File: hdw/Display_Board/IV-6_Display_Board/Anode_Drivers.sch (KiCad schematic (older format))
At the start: 48 parts

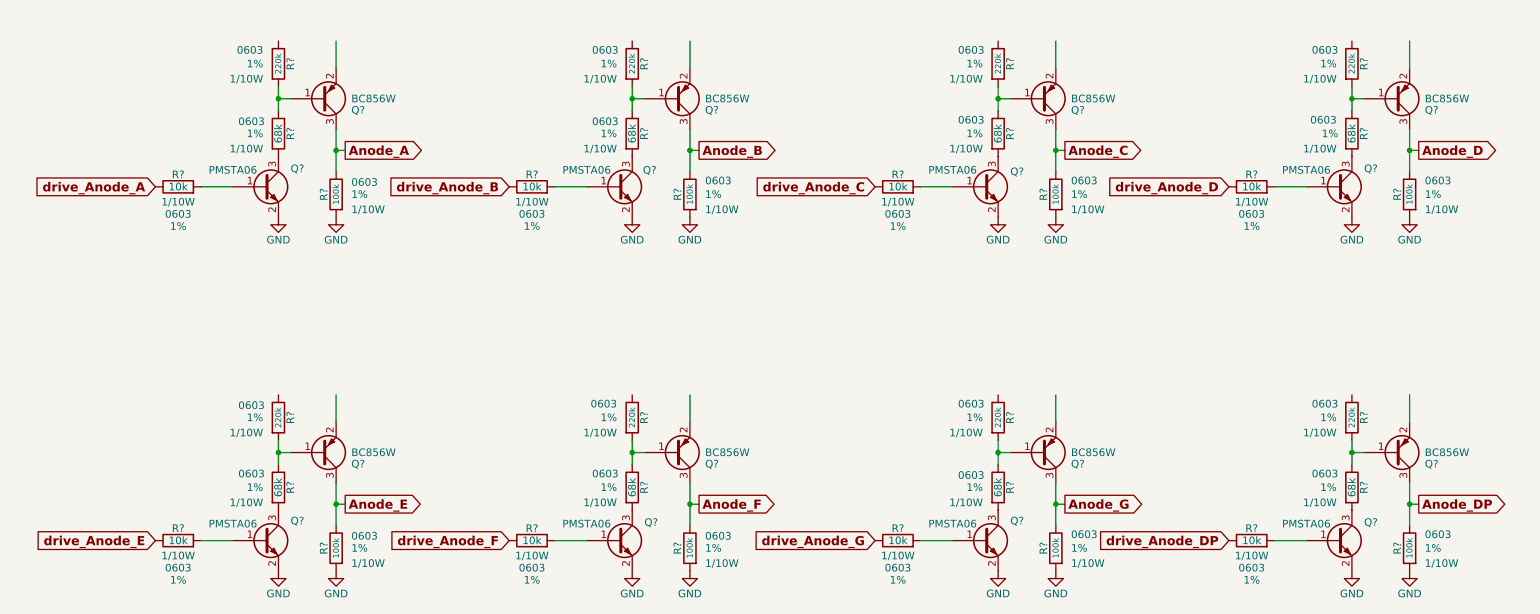
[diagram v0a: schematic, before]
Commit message: Started IV-6 display board, continued logic board development
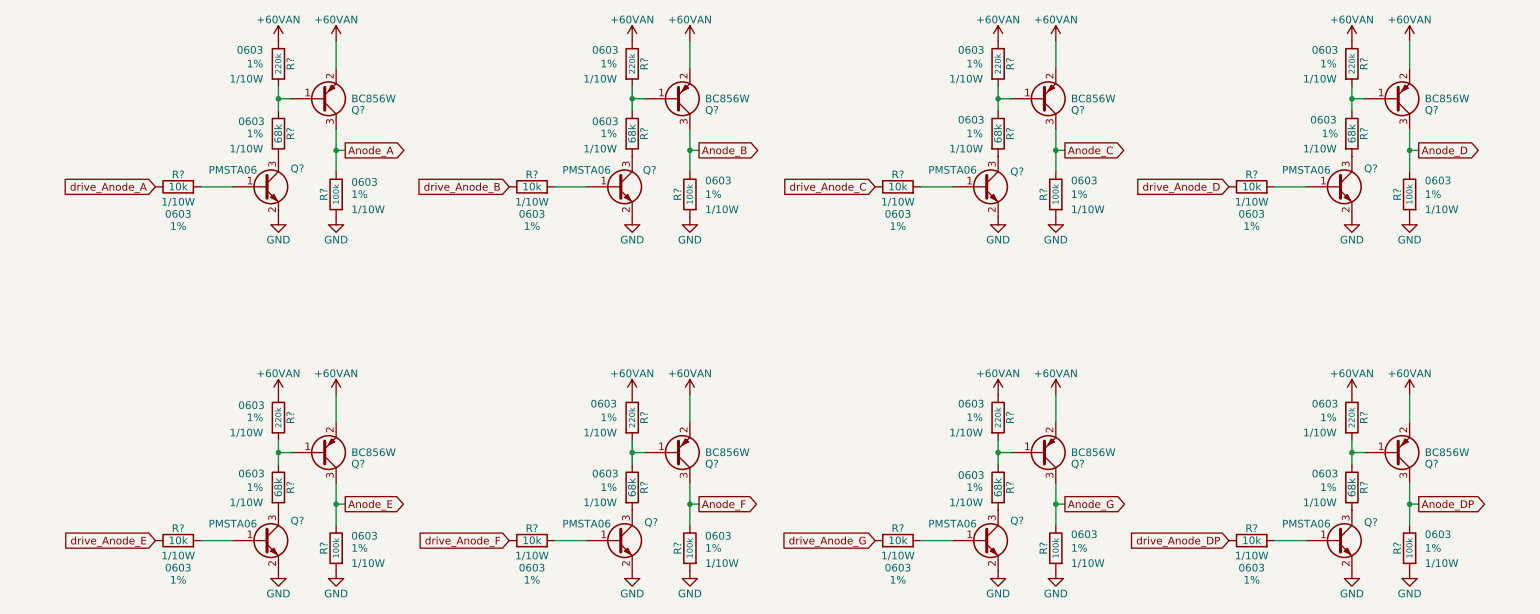
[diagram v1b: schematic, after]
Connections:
- net labels added: +60VAN
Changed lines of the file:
@@
 EESchema Schematic File Version 4
-EELAYER 29 0
+EELAYER 30 0
 EELAYER END
 $Descr A 11000 8500
 encoding utf-8
-Sheet 2 3
+Sheet 2 5
 Title "VFD Clock"
 Date "2019-04-11"
@@
 Wire Wire Line
 	1800 2500 1590 2500
-Text GLabel 1290 2500 0    60   Input ~ 12
+Text GLabel 1290 2500 0    50   Input ~ 0
 drive_Anode_A
-Text GLabel 3620 2500 0    60   Input ~ 12
+Text GLabel 3620 2500 0    50   Input ~ 0
 drive_Anode_B
-Text GLabel 6030 2500 0    60   Input ~ 12
+Text GLabel 6030 2500 0    50   Input ~ 0
 drive_Anode_C
-Text GLabel 8360 2500 0    60   Input ~ 12
+Text GLabel 8360 2500 0    50   Input ~ 0
 drive_Anode_D
-Text GLabel 1290 4830 0    60   Input ~ 12
+Text GLabel 1290 4830 0    50   Input ~ 0
 drive_Anode_E
-Text GLabel 3620 4830 0    60   Input ~ 12
+Text GLabel 3620 4830 0    50   Input ~ 0
 drive_Anode_F
-Text GLabel 6030 4830 0    60   Input ~ 12
+Text GLabel 6030 4830 0    50   Input ~ 0
 drive_Anode_G
-Text GLabel 8360 4830 0    60   Input ~ 12
+Text GLabel 8360 4830 0    50   Input ~ 0
 drive_Anode_DP
-Text GLabel 2540 2260 2    60   Output ~ 12
-Anode_A
 Wire Wire Line
 	2540 2260 2480 2260
@@
 Wire Wire Line
 	4130 2500 3920 2500
-Text GLabel 4870 2260 2    60   Output ~ 12
+Text GLabel 4870 2260 2    50   Output ~ 0
 Anode_B
 Wire Wire Line
@@
 Wire Wire Line
 	6540 2500 6330 2500
-Text GLabel 7280 2260 2    60   Output ~ 12
+Text GLabel 7280 2260 2    50   Output ~ 0
 Anode_C
 Wire Wire Line
@@
 Wire Wire Line
 	8870 2500 8660 2500
-Text GLabel 9610 2260 2    60   Output ~ 12
+Text GLabel 9610 2260 2    50   Output ~ 0
 Anode_D
 Wire Wire Line
@@
 Wire Wire Line
 	1800 4830 1590 4830
-Text GLabel 2540 4590 2    60   Output ~ 12
+Text GLabel 2540 4590 2    50   Output ~ 0
 Anode_E
 Wire Wire Line
@@
 Wire Wire Line
 	4130 4830 3920 4830
-Text GLabel 4870 4590 2    60   Output ~ 12
+Text GLabel 4870 4590 2    50   Output ~ 0
 Anode_F
 Wire Wire Line
@@
 Wire Wire Line
 	6540 4830 6330 4830
-Text GLabel 7280 4590 2    60   Output ~ 12
+Text GLabel 7280 4590 2    50   Output ~ 0
 Anode_G
 Wire Wire Line
@@
 Wire Wire Line
 	8870 4830 8660 4830
-Text GLabel 9610 4590 2    60   Output ~ 12
+Text GLabel 9610 4590 2    50   Output ~ 0
 Anode_DP
 Wire Wire Line
@@
 Wire Wire Line
 	9550 4590 9550 4450
+Text GLabel 2540 2260 2    50   Output ~ 0
+Anode_A
+$Comp
+L Custom_Library:+60VAN #PWR?
+U 1 1 5E0985F3
+P 2100 1540
+F 0 "#PWR?" H 2100 1390 50  0001 C CNN
+F 1 "+60VAN" H 2100 1680 50  0000 C CNN
+F 2 "" H 2100 1540 50  0000 C CNN
+F 3 "" H 2100 1540 50  0000 C CNN
+	1    2100 1540
+	1    0    0    -1
+$EndComp
+$Comp
+L Custom_Library:+60VAN #PWR?
+U 1 1 5E098FFE
+P 2480 1540
+F 0 "#PWR?" H 2480 1390 50  0001 C CNN
+F 1 "+60VAN" H 2480 1680 50  0000 C CNN
+F 2 "" H 2480 1540 50  0000 C CNN
+F 3 "" H 2480 1540 50  0000 C CNN
+	1    2480 1540
+	1    0    0    -1
+$EndComp
+$Comp
+L Custom_Library:+60VAN #PWR?
+U 1 1 5E09967E
+P 4430 1540
+F 0 "#PWR?" H 4430 1390 50  0001 C CNN
+F 1 "+60VAN" H 4430 1680 50  0000 C CNN
+F 2 "" H 4430 1540 50  0000 C CNN
+F 3 "" H 4430 1540 50  0000 C CNN
+	1    4430 1540
+	1    0    0    -1
+$EndComp
+$Comp
+L Custom_Library:+60VAN #PWR?
+U 1 1 5E099BB3
+P 4810 1540
+F 0 "#PWR?" H 4810 1390 50  0001 C CNN
+F 1 "+60VAN" H 4810 1680 50  0000 C CNN
+F 2 "" H 4810 1540 50  0000 C CNN
+F 3 "" H 4810 1540 50  0000 C CNN
+	1    4810 1540
+	1    0    0    -1
+$EndComp
+$Comp
+L Custom_Library:+60VAN #PWR?
+U 1 1 5E099F99
+P 6840 1540
+F 0 "#PWR?" H 6840 1390 50  0001 C CNN
+F 1 "+60VAN" H 6840 1680 50  0000 C CNN
+F 2 "" H 6840 1540 50  0000 C CNN
+F 3 "" H 6840 1540 50  0000 C CNN
+	1    6840 1540
+	1    0    0    -1
+$EndComp
+$Comp
+L Custom_Library:+60VAN #PWR?
+U 1 1 5E09A4A2
+P 7220 1540
+F 0 "#PWR?" H 7220 1390 50  0001 C CNN
+F 1 "+60VAN" H 7220 1680 50  0000 C CNN
+F 2 "" H 7220 1540 50  0000 C CNN
+F 3 "" H 7220 1540 50  0000 C CNN
+	1    7220 1540
+	1    0    0    -1
+$EndComp
+$Comp
+L Custom_Library:+60VAN #PWR?
+U 1 1 5E09A854
+P 9170 1540
+F 0 "#PWR?" H 9170 1390 50  0001 C CNN
+F 1 "+60VAN" H 9170 1680 50  0000 C CNN
+F 2 "" H 9170 1540 50  0000 C CNN
+F 3 "" H 9170 1540 50  0000 C CNN
+	1    9170 1540
+	1    0    0    -1
+$EndComp
+$Comp
+L Custom_Library:+60VAN #PWR?
+U 1 1 5E09ACD4
+P 9550 1540
+F 0 "#PWR?" H 9550 1390 50  0001 C CNN
+F 1 "+60VAN" H 9550 1680 50  0000 C CNN
+F 2 "" H 9550 1540 50  0000 C CNN
+F 3 "" H 9550 1540 50  0000 C CNN
+	1    9550 1540
+	1    0    0    -1
+$EndComp
+$Comp
+L Custom_Library:+60VAN #PWR?
+U 1 1 5E09B095
+P 9550 3870
+F 0 "#PWR?" H 9550 3720 50  0001 C CNN
+F 1 "+60VAN" H 9550 4010 50  0000 C CNN
+F 2 "" H 9550 3870 50  0000 C CNN
+F 3 "" H 9550 3870 50  0000 C CNN
+	1    9550 3870
+	1    0    0    -1
+$EndComp
+$Comp
+L Custom_Library:+60VAN #PWR?
+U 1 1 5E09B6D8
+P 9170 3870
+F 0 "#PWR?" H 9170 3720 50  0001 C CNN
+F 1 "+60VAN" H 9170 4010 50  0000 C CNN
+F 2 "" H 9170 3870 50  0000 C CNN
+F 3 "" H 9170 3870 50  0000 C CNN
+	1    9170 3870
+	1    0    0    -1
+$EndComp
+$Comp
+L Custom_Library:+60VAN #PWR?
+U 1 1 5E09BA28
+P 7220 3870
+F 0 "#PWR?" H 7220 3720 50  0001 C CNN
+F 1 "+60VAN" H 7220 4010 50  0000 C CNN
+F 2 "" H 7220 3870 50  0000 C CNN
+F 3 "" H 7220 3870 50  0000 C CNN
+	1    7220 3870
+	1    0    0    -1
+$EndComp
+$Comp
+L Custom_Library:+60VAN #PWR?
+U 1 1 5E09BF92
+P 6840 3870
+F 0 "#PWR?" H 6840 3720 50  0001 C CNN
+F 1 "+60VAN" H 6840 4010 50  0000 C CNN
+F 2 "" H 6840 3870 50  0000 C CNN
+F 3 "" H 6840 3870 50  0000 C CNN
+	1    6840 3870
+	1    0    0    -1
+$EndComp
+$Comp
+L Custom_Library:+60VAN #PWR?
+U 1 1 5E09C220
+P 4810 3870
+F 0 "#PWR?" H 4810 3720 50  0001 C CNN
+F 1 "+60VAN" H 4810 4010 50  0000 C CNN
+F 2 "" H 4810 3870 50  0000 C CNN
+F 3 "" H 4810 3870 50  0000 C CNN
+	1    4810 3870
+	1    0    0    -1
+$EndComp
+$Comp
+L Custom_Library:+60VAN #PWR?
+U 1 1 5E09C8C7
+P 4430 3870
+F 0 "#PWR?" H 4430 3720 50  0001 C CNN
+F 1 "+60VAN" H 4430 4010 50  0000 C CNN
+F 2 "" H 4430 3870 50  0000 C CNN
+F 3 "" H 4430 3870 50  0000 C CNN
+	1    4430 3870
+	1    0    0    -1
+$EndComp
+$Comp
+L Custom_Library:+60VAN #PWR?
+U 1 1 5E09CAE0
+P 2480 3870
+F 0 "#PWR?" H 2480 3720 50  0001 C CNN
+F 1 "+60VAN" H 2480 4010 50  0000 C CNN
+F 2 "" H 2480 3870 50  0000 C CNN
+F 3 "" H 2480 3870 50  0000 C CNN
+	1    2480 3870
+	1    0    0    -1
+$EndComp
+$Comp
+L Custom_Library:+60VAN #PWR?
+U 1 1 5E09D038
+P 2100 3870
+F 0 "#PWR?" H 2100 3720 50  0001 C CNN
+F 1 "+60VAN" H 2100 4010 50  0000 C CNN
+F 2 "" H 2100 3870 50  0000 C CNN
+F 3 "" H 2100 3870 50  0000 C CNN
+	1    2100 3870
+	1    0    0    -1
+$EndComp
 $EndSCHEMATC

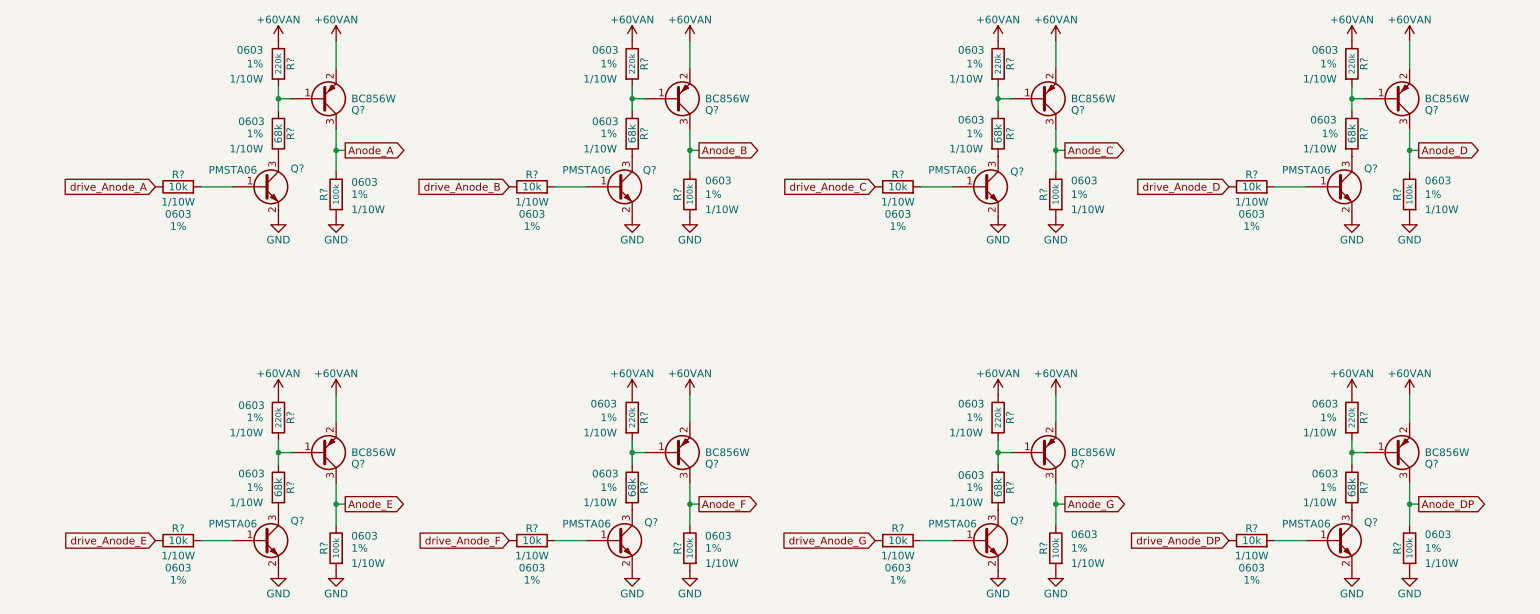
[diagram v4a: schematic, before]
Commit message: Reorganized logic board pages
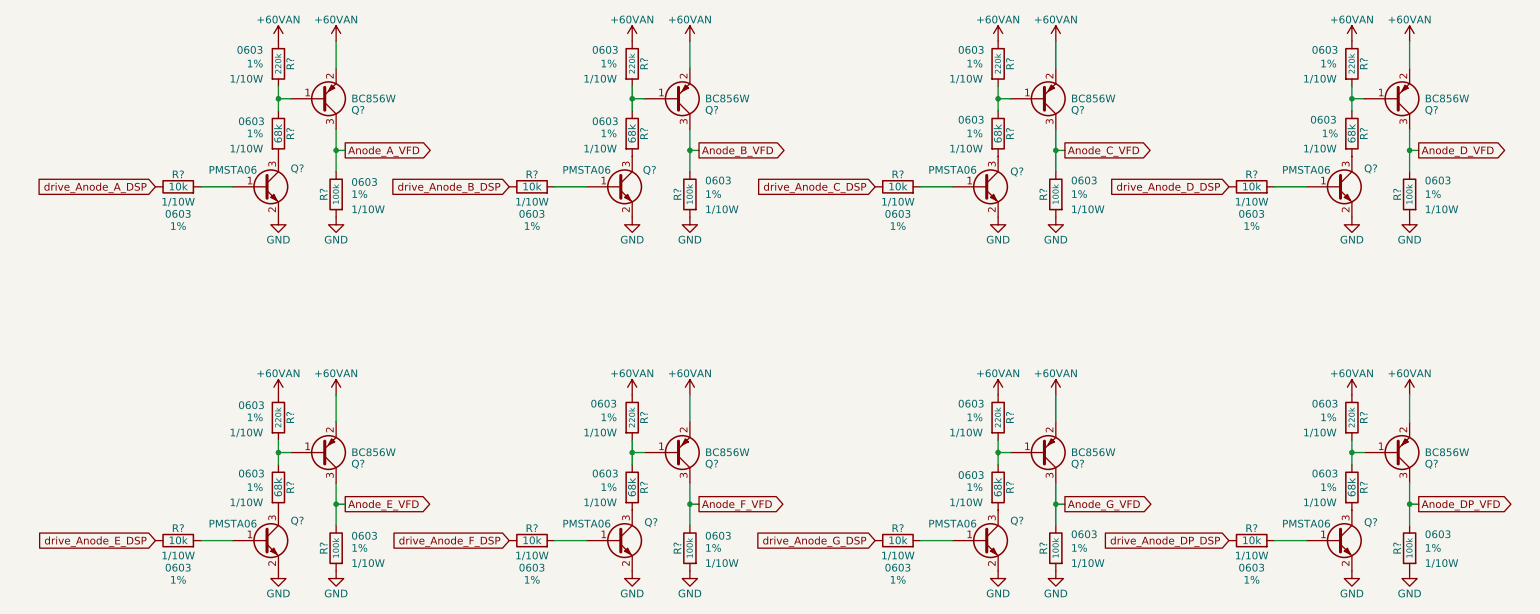
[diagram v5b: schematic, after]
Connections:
- net Anode_A renamed Anode_A_VFD
- net Anode_B renamed Anode_B_VFD
- net Anode_C renamed Anode_C_VFD
- net Anode_D renamed Anode_D_VFD
- net Anode_DP renamed Anode_DP_VFD
- net Anode_E renamed Anode_E_VFD
- net Anode_F renamed Anode_F_VFD
- net Anode_G renamed Anode_G_VFD
- net drive_Anode_A renamed drive_Anode_A_DSP
- net drive_Anode_B renamed drive_Anode_B_DSP
- net drive_Anode_C renamed drive_Anode_C_DSP
- net drive_Anode_D renamed drive_Anode_D_DSP
- net drive_Anode_DP renamed drive_Anode_DP_DSP
- net drive_Anode_E renamed drive_Anode_E_DSP
- net drive_Anode_F renamed drive_Anode_F_DSP
- net drive_Anode_G renamed drive_Anode_G_DSP
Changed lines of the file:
@@
 	1800 2500 1590 2500
 Text GLabel 1290 2500 0    50   Input ~ 0
-drive_Anode_A
+drive_Anode_A_DSP
 Text GLabel 3620 2500 0    50   Input ~ 0
-drive_Anode_B
+drive_Anode_B_DSP
 Text GLabel 6030 2500 0    50   Input ~ 0
-drive_Anode_C
+drive_Anode_C_DSP
 Text GLabel 8360 2500 0    50   Input ~ 0
-drive_Anode_D
+drive_Anode_D_DSP
 Text GLabel 1290 4830 0    50   Input ~ 0
-drive_Anode_E
+drive_Anode_E_DSP
 Text GLabel 3620 4830 0    50   Input ~ 0
-drive_Anode_F
+drive_Anode_F_DSP
 Text GLabel 6030 4830 0    50   Input ~ 0
-drive_Anode_G
+drive_Anode_G_DSP
 Text GLabel 8360 4830 0    50   Input ~ 0
-drive_Anode_DP
+drive_Anode_DP_DSP
 Wire Wire Line
 	2540 2260 2480 2260
@@
 	4130 2500 3920 2500
 Text GLabel 4870 2260 2    50   Output ~ 0
-Anode_B
+Anode_B_VFD
 Wire Wire Line
 	4870 2260 4810 2260
@@
 	6540 2500 6330 2500
 Text GLabel 7280 2260 2    50   Output ~ 0
-Anode_C
+Anode_C_VFD
 Wire Wire Line
 	7280 2260 7220 2260
@@
 	8870 2500 8660 2500
 Text GLabel 9610 2260 2    50   Output ~ 0
-Anode_D
+Anode_D_VFD
 Wire Wire Line
 	9610 2260 9550 2260
@@
 	1800 4830 1590 4830
 Text GLabel 2540 4590 2    50   Output ~ 0
-Anode_E
+Anode_E_VFD
 Wire Wire Line
 	2540 4590 2480 4590
@@
 Wire Wire Line
 	4130 4830 3920 4830
-Text GLabel 4870 4590 2    50   Output ~ 0
-Anode_F
 Wire Wire Line
 	4870 4590 4810 4590
@@
 	6540 4830 6330 4830
 Text GLabel 7280 4590 2    50   Output ~ 0
-Anode_G
+Anode_G_VFD
 Wire Wire Line
 	7280 4590 7220 4590
@@
 	8870 4830 8660 4830
 Text GLabel 9610 4590 2    50   Output ~ 0
-Anode_DP
+Anode_DP_VFD
 Wire Wire Line
 	9610 4590 9550 4590
@@
 	9550 4590 9550 4450
 Text GLabel 2540 2260 2    50   Output ~ 0
-Anode_A
+Anode_A_VFD
 $Comp
 L Custom_Library:+60VAN #PWR?
@@
 	1    0    0    -1
 $EndComp
+Text GLabel 4870 4590 2    50   Output ~ 0
+Anode_F_VFD
 $EndSCHEMATC

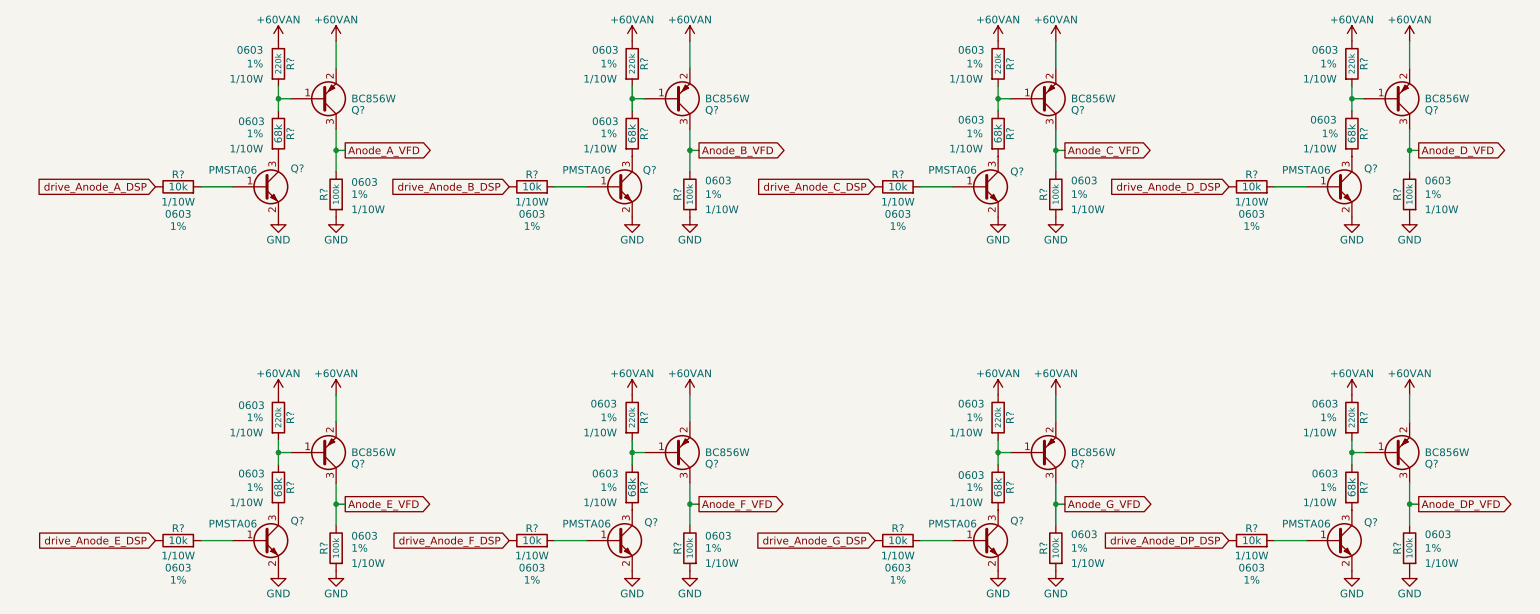
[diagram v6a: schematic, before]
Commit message: Started display board PCB
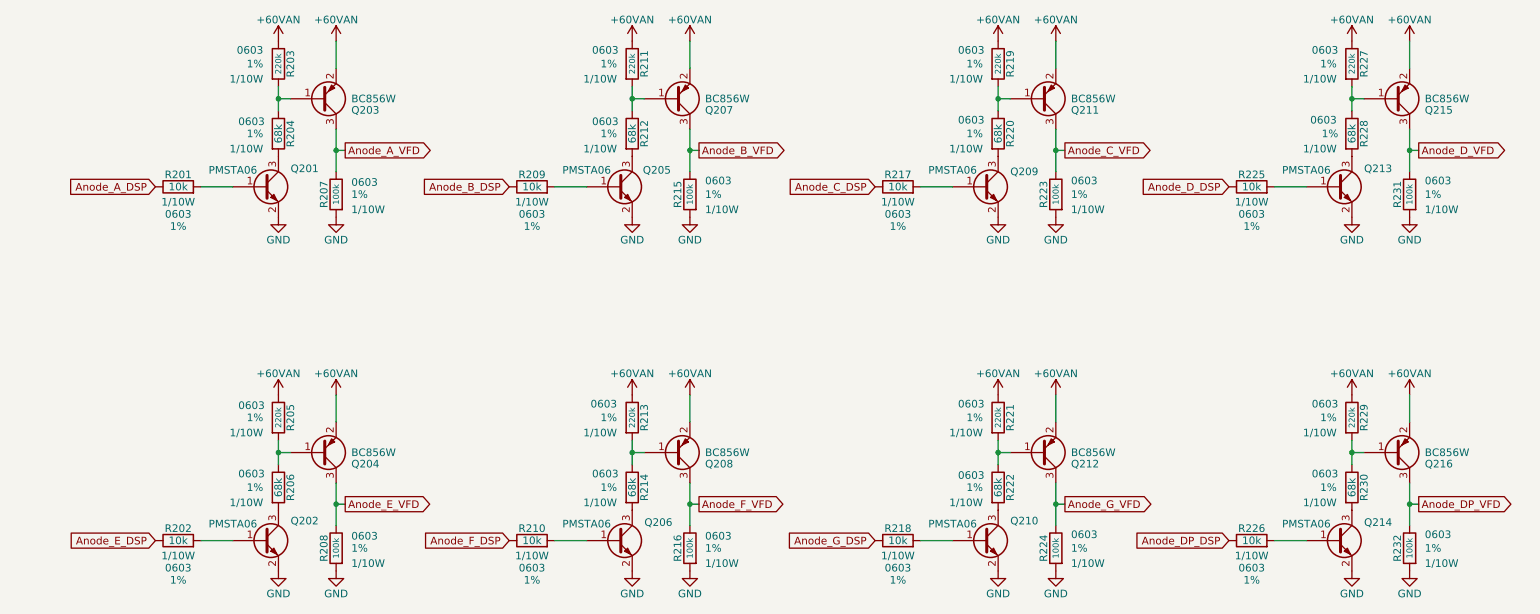
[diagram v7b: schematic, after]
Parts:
- Q201, Q202, Q203, Q204, Q205, Q206, Q207, Q208, Q209, Q210, Q211, Q212, Q213, Q214, Q215, Q216: renamed from Q?; footprint TO_SOT_Packages_SMD:SOT-323 -> TO_SOT_Packages_SMD:SOT-323_SC-70
- gave numbers to parts that had none: 32
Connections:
- net drive_Anode_A_DSP renamed Anode_A_DSP
- net drive_Anode_B_DSP renamed Anode_B_DSP
- net drive_Anode_C_DSP renamed Anode_C_DSP
- net drive_Anode_DP_DSP renamed Anode_DP_DSP
- net drive_Anode_D_DSP renamed Anode_D_DSP
- net drive_Anode_E_DSP renamed Anode_E_DSP
- net drive_Anode_F_DSP renamed Anode_F_DSP
- net drive_Anode_G_DSP renamed Anode_G_DSP
